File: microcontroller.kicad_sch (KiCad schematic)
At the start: 54 parts, among them SW1 SW_SPST, SW2 SW_SPST, U3 W25Q16JVSS, U4 W25Q16JVSS, U6 RP2040, Y1 12MHz/10pF, Y2 12MHz/10pF

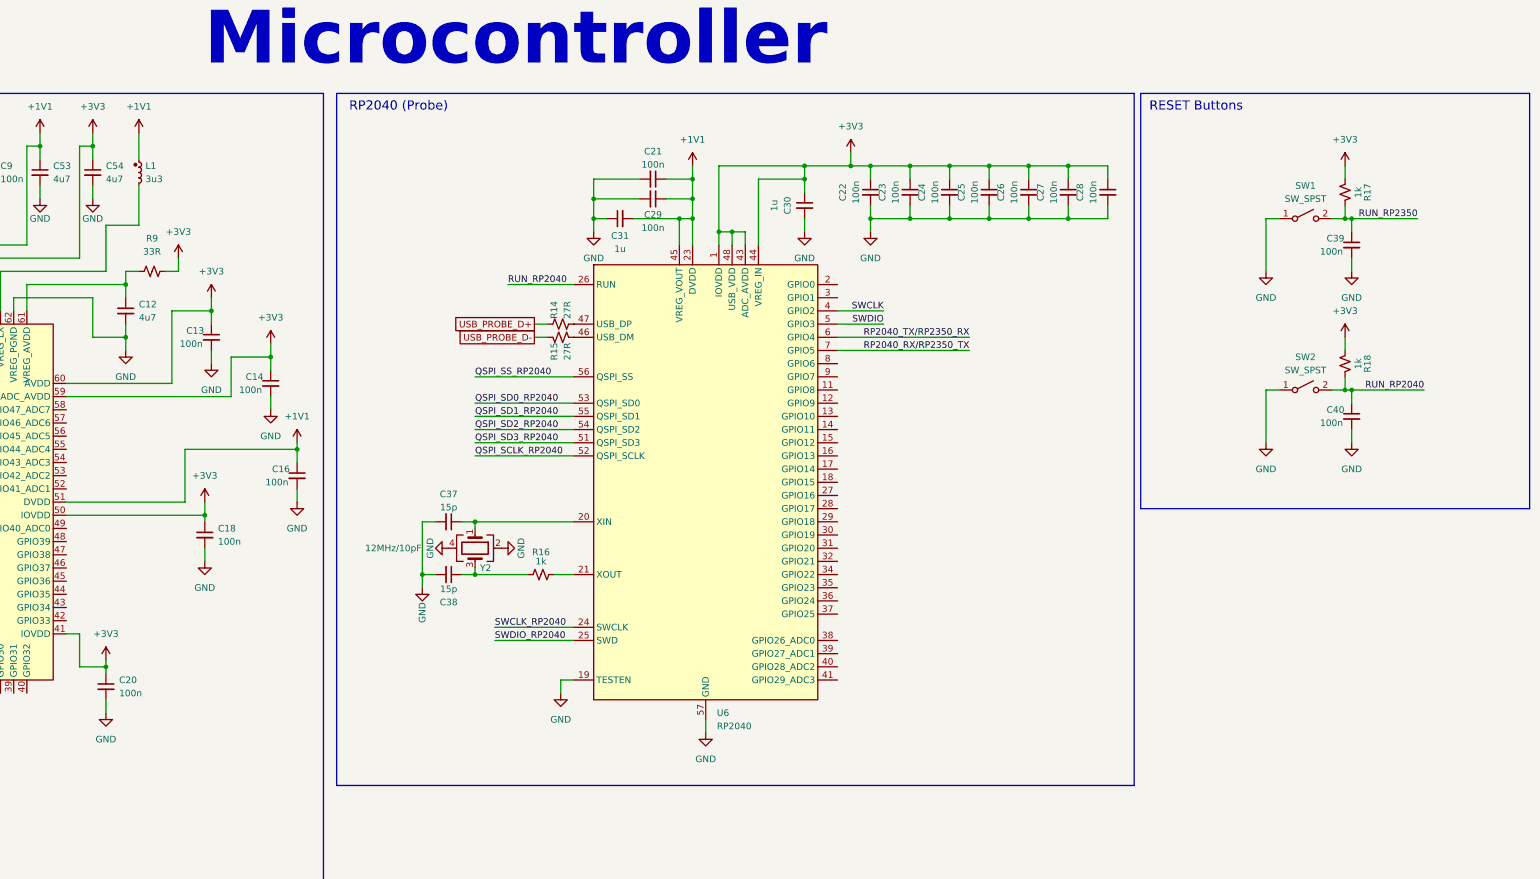
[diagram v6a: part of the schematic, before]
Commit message: feat: adds pin headers
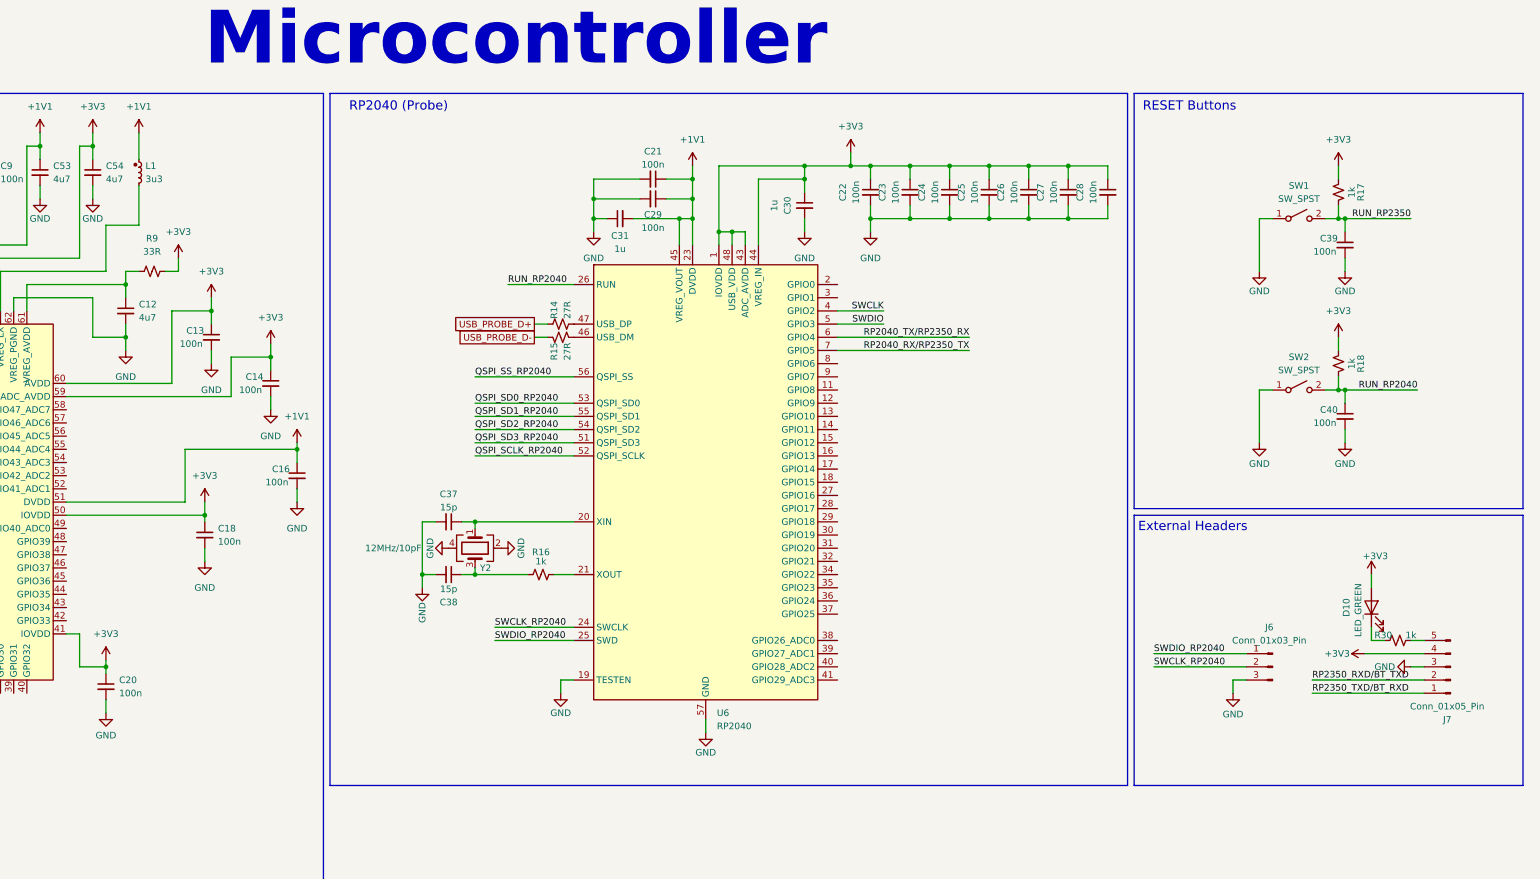
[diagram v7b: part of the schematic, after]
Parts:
- added D10: LED_GREEN, LED_SMD:LED_0603_1608Metric, symbol Device:LED
- added J6: Conn_01x03_Pin, Connector:FanPinHeader_1x03_P2.54mm_Vertical, symbol Connector:Conn_01x03_Pin
- added J7: Conn_01x05_Pin, Connector_PinHeader_2.54mm:PinHeader_1x05_P2.54mm_Vertical, symbol Connector:Conn_01x05_Pin
- added R30: 1k, Resistor_SMD:R_0402_1005Metric, symbol Device:R_Small_US
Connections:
- net +3V3: now also D10.2 (A), J7.4 (Pin_4)
- net GND: now also J6.3 (Pin_3), J7.3 (Pin_3)
- net SWCLK_RP2040: now also J6.2 (Pin_2)
- net SWDIO_RP2040: now also J6.1 (Pin_1)
- new net: D10.1 (K), R30.1
- new net: J7.5 (Pin_5), R30.2
- new net RP2350_RXD/BT_TXD: J7.2 (Pin_2)
- new net RP2350_TXD/BT_RXD: J7.1 (Pin_1)
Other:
- note added: "External Headers"
- moved on the sheet: C39, C40, R17, R18, SW1, SW2

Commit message: feat: connects SPI and I2C pins to MCU
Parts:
- R17, R18: now not fitted
- U6: footprint Package_DFN_QFN:QFN-56-1EP_7x7mm_P0.4mm_EP3.2x3.2mm -> Package_DFN_QFN:QFN-56-1EP_7x7mm_P0.4mm_EP3.2x3.2mm_ThermalVias
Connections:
- net SD_CD/DAT3: now also U5.48 (GPIO39); no longer U5.14 (GPIO15)
- net SD_CLK: now also U5.43 (GPIO34); no longer U5.8 (GPIO10)
- net SD_CMD: now also U5.44 (GPIO35); no longer U5.9 (GPIO11)
- net SD_DAT0: now also U5.45 (GPIO36); no longer U5.11 (GPIO12)
- net SD_DAT1: now also U5.46 (GPIO37); no longer U5.12 (GPIO13)
- net SD_DAT2: now also U5.47 (GPIO38); no longer U5.13 (GPIO14)
- net I2C_SDA: now reaches U5.1 (GPIO4)
- net ACCEL_INT1: now reaches U5.16 (GPIO16)
- net ACCEL_INT2: now reaches U5.17 (GPIO17)
- net I2C_SCL: now reaches U5.2 (GPIO5)
- net POTENTIOMETER2_ADC: now reaches U5.53 (GPIO42_ADC2)
- net POTENTIOMETER1_ADC: now reaches U5.55 (GPIO44_ADC4)
- net LDR_ADC: now reaches U5.57 (GPIO46_ADC6)
- net RP2040_RX/RP2350_TX renamed RP2350_TX/RP2040_RX
- net RP2040_TX/RP2350_RX renamed RP2350_RX/RP2040_TX
- net RP2350_RXD/BT_TXD renamed RP2350_RX/BT_TX
- net RP2350_TXD/BT_RXD renamed RP2350_TX/BT_RX
- new net SPI_ACCEL_CS: U5.12 (GPIO13)
- new net SPI_MISO: U5.11 (GPIO12)
- new net SPI_MOSI: U5.14 (GPIO15)
- new net SPI_SCLK: U5.13 (GPIO14)
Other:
- moved on the sheet: C18, C19
